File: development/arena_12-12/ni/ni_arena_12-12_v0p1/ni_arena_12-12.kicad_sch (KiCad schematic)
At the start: 0 parts

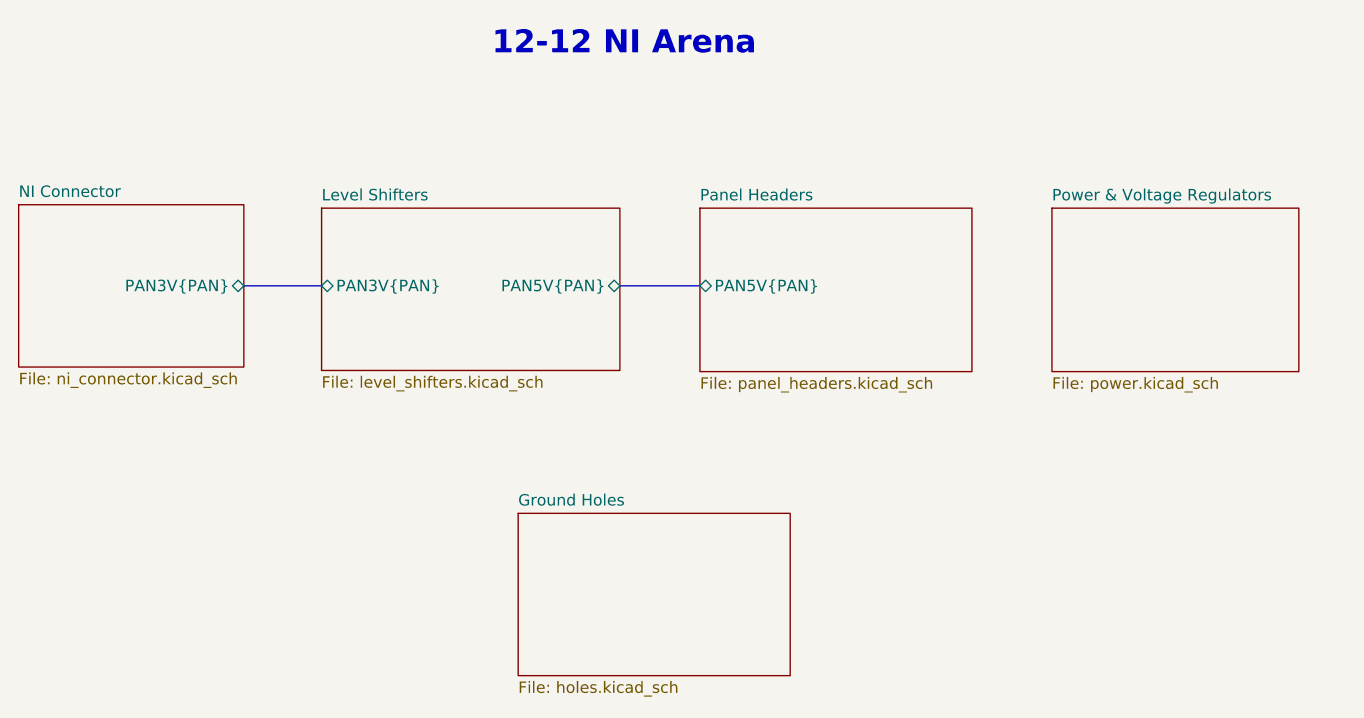
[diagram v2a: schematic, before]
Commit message: Worked on NI 12-12 arena schematic.
Set up new bus definitions and started working through DRC issues.
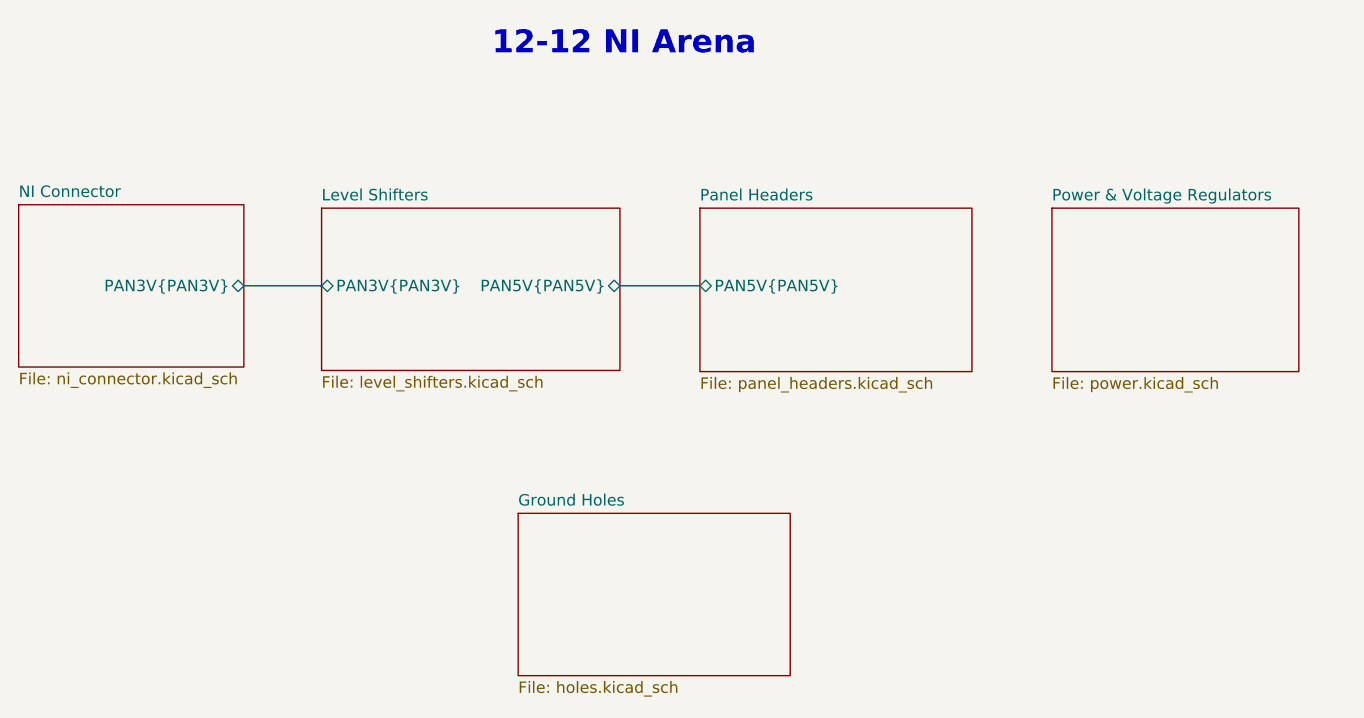
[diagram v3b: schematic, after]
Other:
- sheet Level Shifters ports: added PAN3V{PAN3V}, PAN5V{PAN5V}; removed PAN3V{PAN}, PAN5V{PAN}
- sheet NI Connector ports: added PAN3V{PAN3V}; removed PAN3V{PAN}
- sheet Panel Headers ports: added PAN5V{PAN5V}; removed PAN5V{PAN}
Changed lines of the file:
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@@
 			)
 		)
-		(pin "PAN5V{PAN}" bidirectional
+		(pin "PAN5V{PAN5V}" bidirectional
 			(at 127.254 58.42 0)
 			(effects
@@
 			)
 		)
-		(pin "PAN3V{PAN}" bidirectional
+		(pin "PAN3V{PAN3V}" bidirectional
 			(at 94.107 58.42 180)
 			(effects
@@
 			)
 		)
-		(pin "PAN5V{PAN}" bidirectional
+		(pin "PAN5V{PAN5V}" bidirectional
 			(at 136.144 58.42 180)
 			(effects
@@
 			)
 		)
-		(pin "PAN3V{PAN}" bidirectional
+		(pin "PAN3V{PAN3V}" bidirectional
 			(at 85.471 58.42 0)
 			(effects
